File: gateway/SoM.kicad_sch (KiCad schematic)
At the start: 18 parts, among them SW901 Reset, SW902 On / Off, X901 SoM, X902 UART

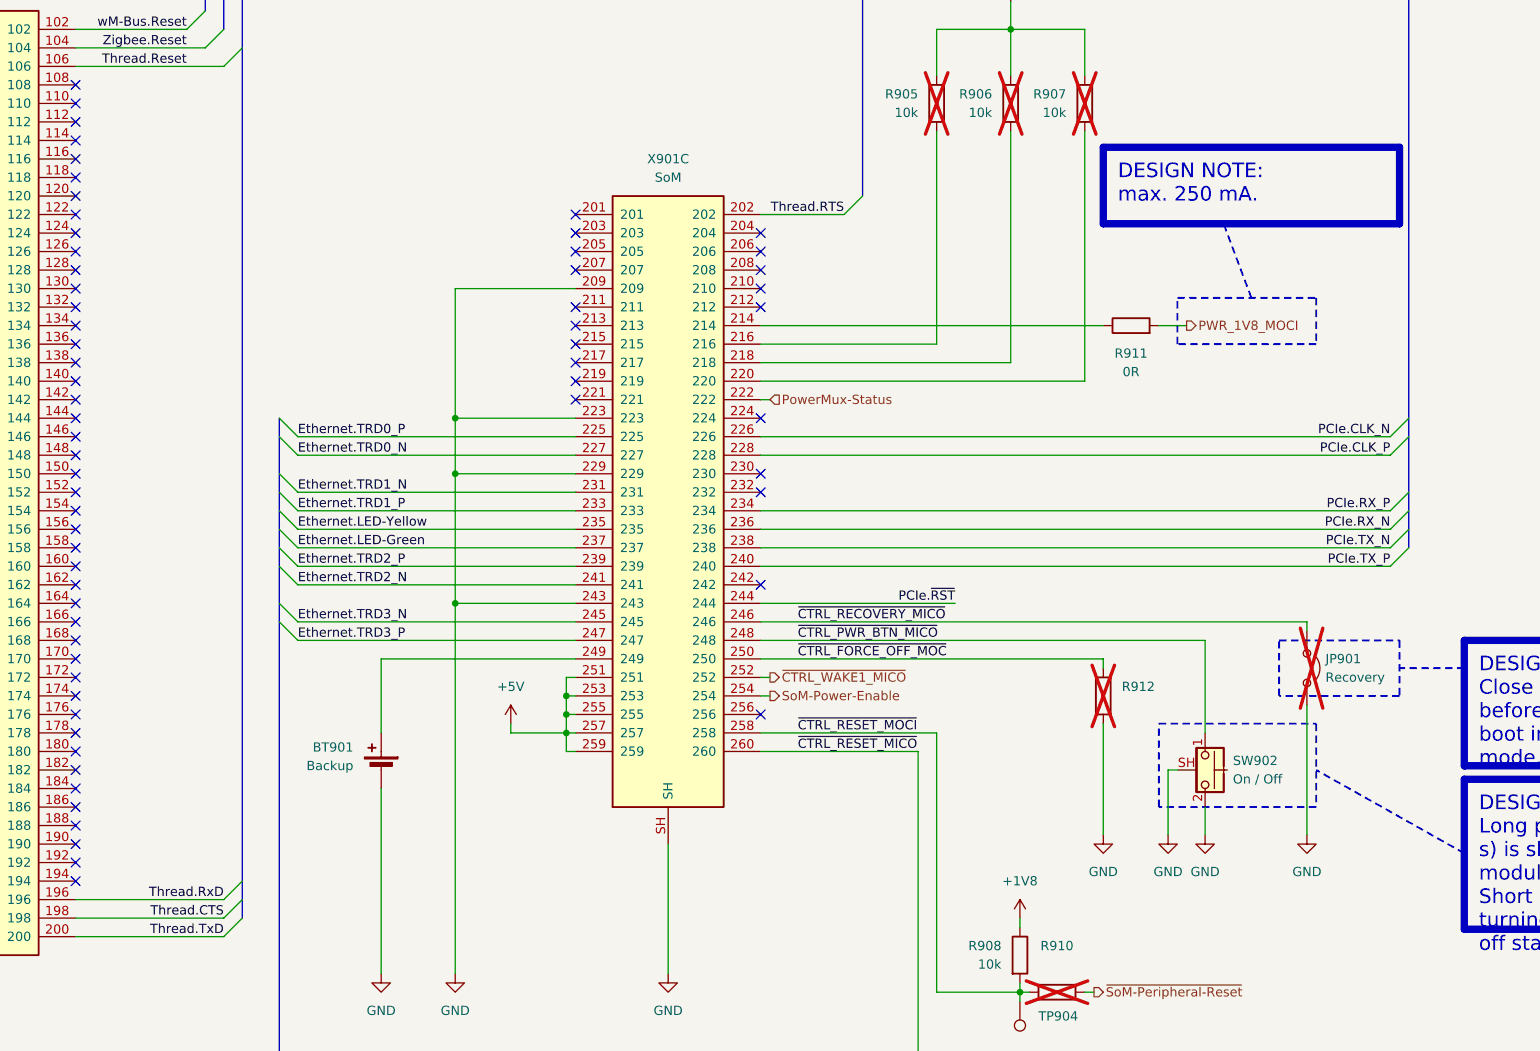
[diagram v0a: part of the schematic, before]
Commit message: Update pin mappings
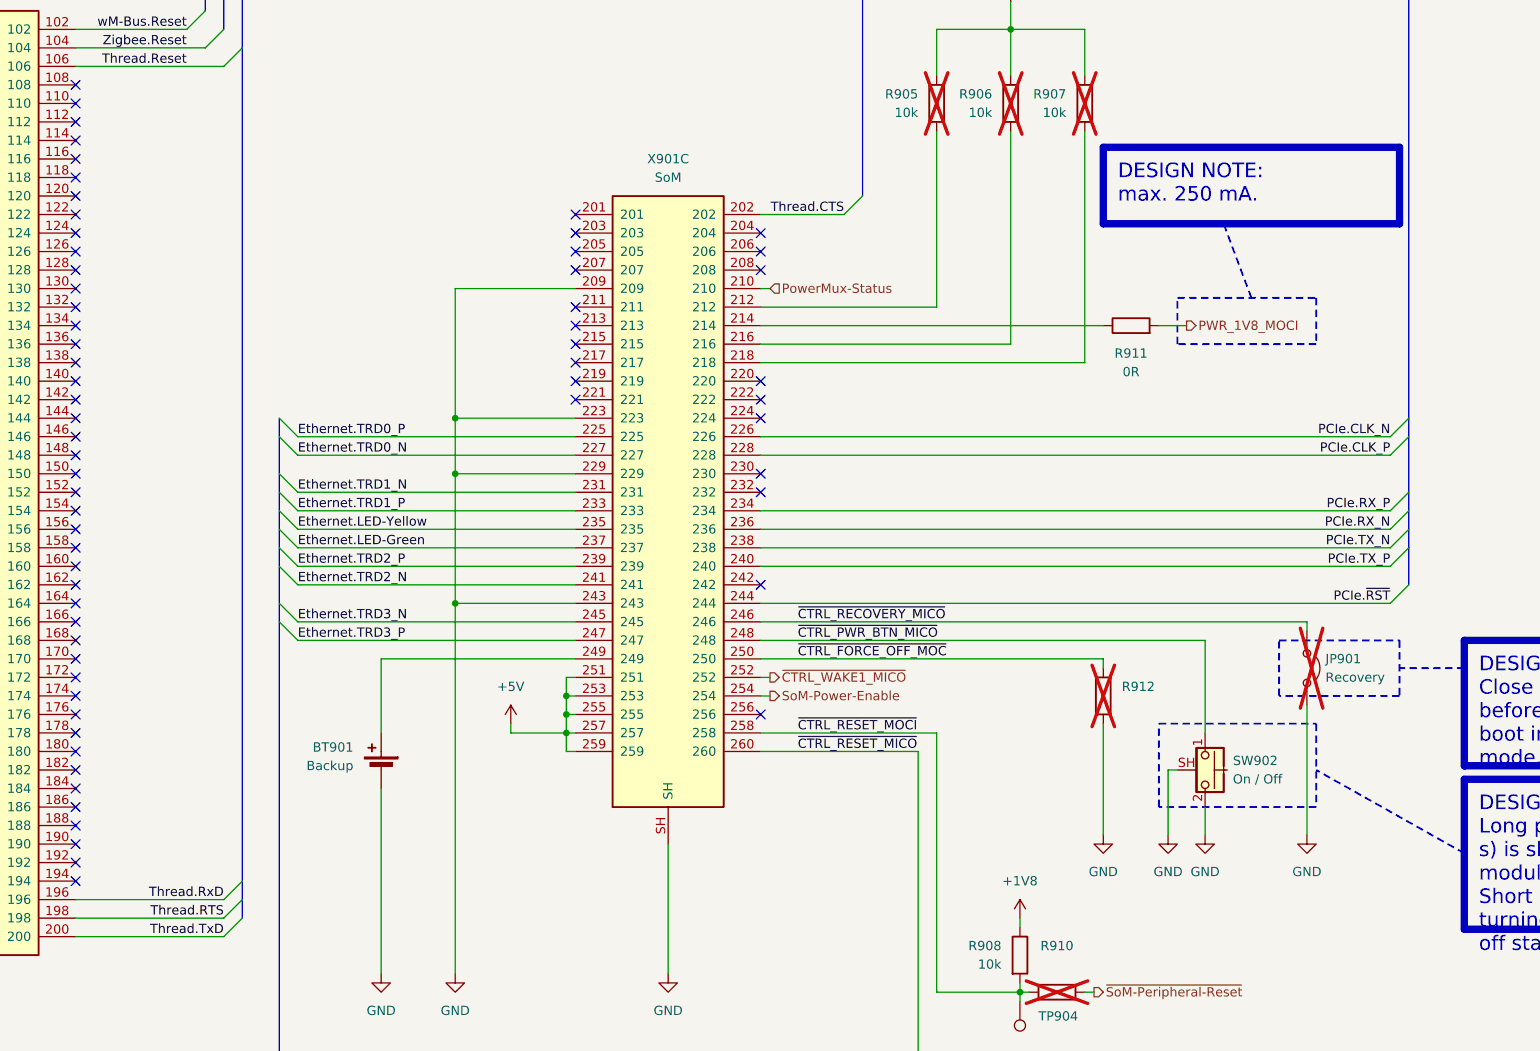
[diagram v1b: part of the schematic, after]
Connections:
- net PowerMux-Status: now also X901.210; no longer X901.222
- net Thread.CTS: now also X901.202; no longer X901.198
- net Thread.RTS: now also X901.198; no longer X901.202
- net at R906.2: now also X901.216; no longer X901.218
- net at X901.212: now also R905.2
- net at R907.2: now also X901.218; no longer X901.220
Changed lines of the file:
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@@
 	)
 	(no_connect
+		(at 267.97 118.11)
+	)
+	(no_connect
 		(at 58.42 107.95)
 	)
@@
 	)
 	(no_connect
-		(at 267.97 105.41)
+		(at 267.97 115.57)
 	)
 	(no_connect
@@
 	)
 	(no_connect
-		(at 267.97 102.87)
-	)
-	(no_connect
 		(at 148.59 100.33)
 	)
@@
 	)
 	(bus_entry
+		(at 354.33 146.05)
+		(size 2.54 -2.54)
+		(stroke
+			(width 0)
+			(type default)
+		)
+	)
+	(bus_entry
 		(at 43.18 179.07)
 		(size 2.54 2.54)
@@
 	(wire
 		(pts
-			(xy 267.97 146.05) (xy 294.64 146.05)
+			(xy 267.97 146.05) (xy 354.33 146.05)
 		)
 		(stroke
@@
 		)
 	)
-	(wire
-		(pts
-			(xy 312.42 115.57) (xy 312.42 81.28)
-		)
-		(stroke
-			(width 0)
-			(type default)
-		)
-	)
 	(bus
 		(pts
@@
 	(wire
 		(pts
-			(xy 267.97 113.03) (xy 302.26 113.03)
-		)
-		(stroke
-			(width 0)
-			(type default)
-		)
-	)
-	(wire
-		(pts
 			(xy 83.82 120.65) (xy 85.09 120.65)
 		)
@@
 		)
 	)
-	(wire
+	(bus
 		(pts
-			(xy 204.47 148.59) (xy 242.57 148.59)
+			(xy 356.87 138.43) (xy 356.87 143.51)
 		)
 		(stroke
@@
 	(wire
 		(pts
-			(xy 124.46 130.81) (xy 148.59 130.81)
+			(xy 204.47 148.59) (xy 242.57 148.59)
 		)
 		(stroke
@@
 	(wire
 		(pts
-			(xy 147.32 186.69) (xy 147.32 196.85)
+			(xy 124.46 130.81) (xy 148.59 130.81)
 		)
 		(stroke
@@
 	(wire
 		(pts
-			(xy 147.32 151.13) (xy 147.32 158.75)
+			(xy 147.32 186.69) (xy 147.32 196.85)
 		)
 		(stroke
@@
 	(wire
 		(pts
-			(xy 292.1 110.49) (xy 292.1 81.28)
+			(xy 147.32 151.13) (xy 147.32 158.75)
 		)
 		(stroke
@@
 	(wire
 		(pts
+			(xy 267.97 110.49) (xy 302.26 110.49)
+		)
+		(stroke
+			(width 0)
+			(type default)
+		)
+	)
+	(wire
+		(pts
 			(xy 58.42 80.01) (xy 57.15 80.01)
 		)
@@
 	(wire
 		(pts
+			(xy 312.42 113.03) (xy 312.42 81.28)
+		)
+		(stroke
+			(width 0)
+			(type default)
+		)
+	)
+	(wire
+		(pts
 			(xy 312.42 199.39) (xy 313.69 199.39)
 		)
@@
 		)
 	)
+	(wire
+		(pts
+			(xy 292.1 81.28) (xy 292.1 105.41)
+		)
+		(stroke
+			(width 0)
+			(type default)
+		)
+	)
 	(polyline
 		(pts
@@
 	(wire
 		(pts
+			(xy 267.97 113.03) (xy 312.42 113.03)
+		)
+		(stroke
+			(width 0)
+			(type default)
+		)
+	)
+	(wire
+		(pts
 			(xy 204.47 123.19) (xy 242.57 123.19)
 		)
@@
 	(wire
 		(pts
-			(xy 267.97 118.11) (xy 269.24 118.11)
+			(xy 267.97 102.87) (xy 269.24 102.87)
 		)
 		(stroke
@@
 	(wire
 		(pts
-			(xy 267.97 115.57) (xy 312.42 115.57)
-		)
-		(stroke
-			(width 0)
-			(type default)
-		)
-	)
-	(wire
-		(pts
 			(xy 45.72 181.61) (xy 58.42 181.61)
 		)
@@
 	(wire
 		(pts
-			(xy 173.99 67.31) (xy 189.23 67.31)
+			(xy 302.26 110.49) (xy 302.26 81.28)
 		)
 		(stroke
@@
 	(wire
 		(pts
-			(xy 302.26 113.03) (xy 302.26 81.28)
+			(xy 173.99 67.31) (xy 189.23 67.31)
 		)
 		(stroke
@@
 		)
 	)
+	(wire
+		(pts
+			(xy 267.97 105.41) (xy 292.1 105.41)
+		)
+		(stroke
+			(width 0)
+			(type default)
+		)
+	)
 	(bus
 		(pts
@@
 	(wire
 		(pts
-			(xy 267.97 110.49) (xy 292.1 110.49)
-		)
-		(stroke
-			(width 0)
-			(type default)
-		)
-	)
-	(wire
-		(pts
 			(xy 45.72 87.63) (xy 58.42 87.63)
 		)
@@
 		)
 	)
+	(label "PCIe.~{RST}"
+		(at 354.33 146.05 180)
+		(effects
+			(font
+				(size 1.27 1.27)
+			)
+			(justify right bottom)
+		)
+	)
 	(label "Ethernet.TRD2_N"
 		(at 204.47 143.51 0)
@@
 		)
 	)
-	(label "Thread.CTS"
+	(label "Thread.RTS"
 		(at 194.31 189.23 180)
 		(effects
@@
 		)
 	)
-	(label "PCIe.~{RST}"
-		(at 294.64 146.05 180)
-		(effects
-			(font
-				(size 1.27 1.27)
-			)
-			(justify right bottom)
-		)
-	)
 	(label "PCIe.TX_P"
 		(at 354.33 140.97 180)
@@
 		)
 	)
-	(label "Thread.RTS"
+	(label "Thread.CTS"
 		(at 279.4 92.71 180)
 		(effects
@@
 	(hierarchical_label "PowerMux-Status"
 		(shape input)
-		(at 269.24 118.11 0)
+		(at 269.24 102.87 0)
 		(effects
 			(font

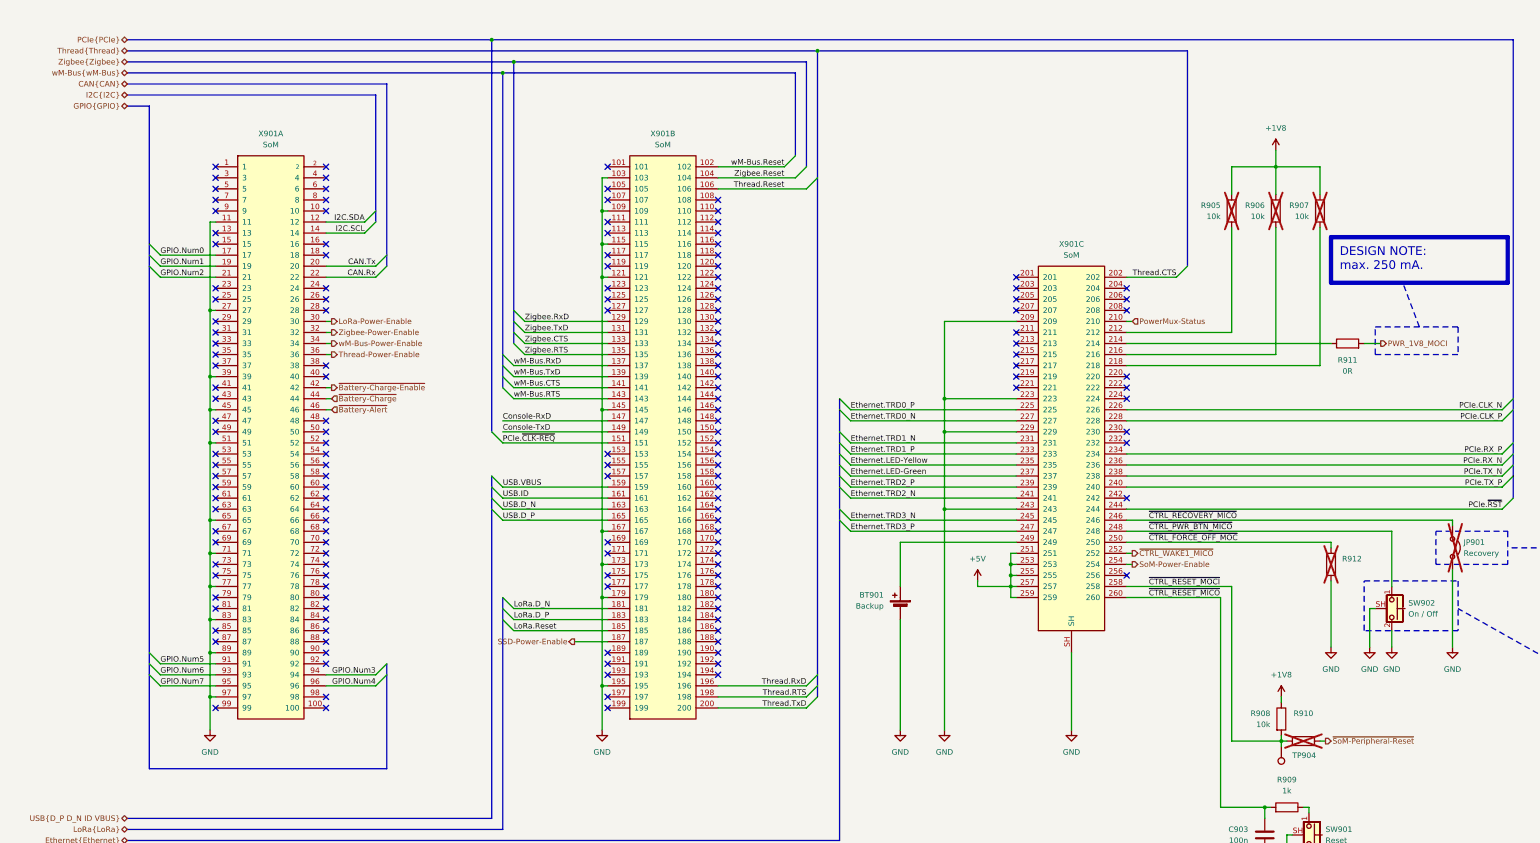
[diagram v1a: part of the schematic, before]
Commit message: Adding level shifter, update documentation
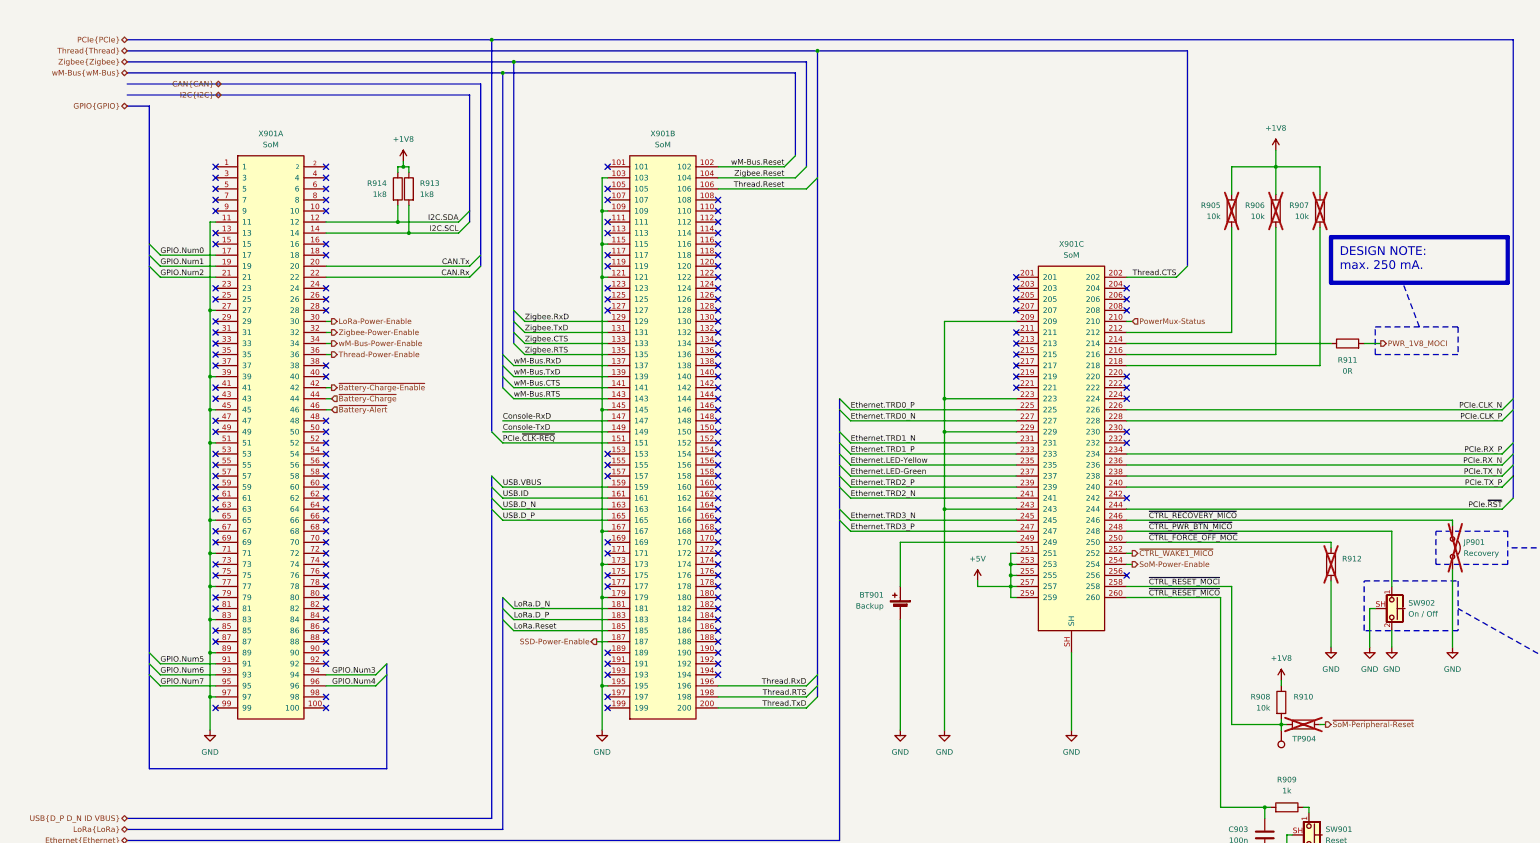
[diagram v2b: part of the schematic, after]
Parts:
- added R913, R914: 1k8, Resistor_SMD:R_0805_2012Metric, symbol Device:R
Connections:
- net +1V8: now also R913.1, R914.1
- net I2C.SCL: now also R913.2
- net I2C.SDA: now also R914.2
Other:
- moved on the sheet: R908, R910, TP904
